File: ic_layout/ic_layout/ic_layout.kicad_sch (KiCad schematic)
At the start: 0 parts

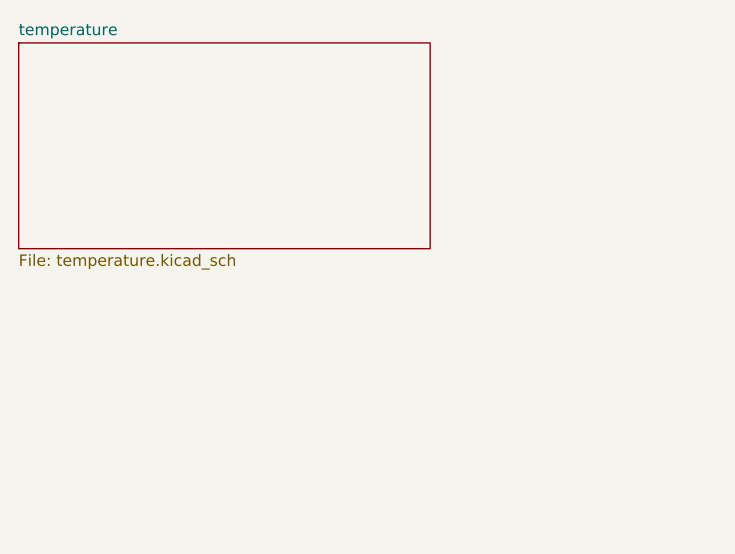
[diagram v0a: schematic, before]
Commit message: - Add XT30 - Add female ring terminal mount - Add 40A SMD fuse
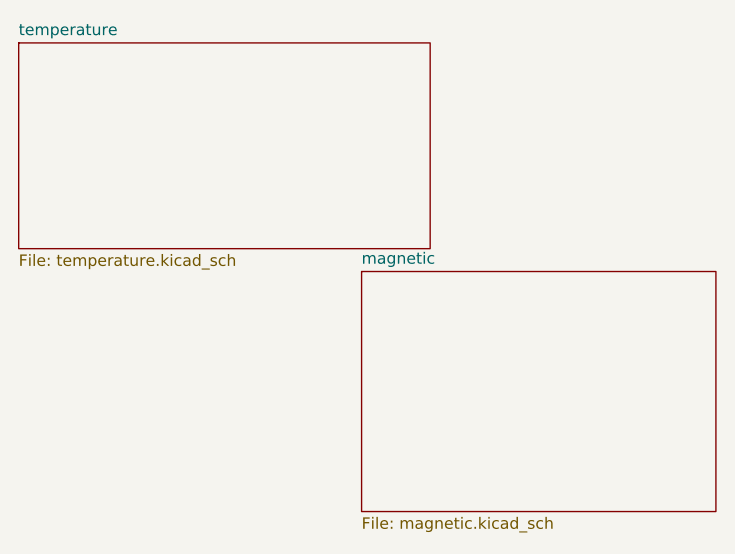
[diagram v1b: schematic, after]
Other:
- added sheet magnetic (magnetic.kicad_sch)
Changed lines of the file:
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@@
 	(paper "A4")
+	(sheet
+		(at 100.33 72.39)
+		(size 39.37 26.67)
+		(exclude_from_sim no)
+		(in_bom yes)
+		(on_board yes)
+		(dnp no)
+		(fields_autoplaced yes)
+		(stroke
+			(width 0.1524)
+			(type solid)
+		)
+		(fill
+			(color 0 0 0 0.0000)
+		)
+		(property "Sheetname" "magnetic"
+			(at 100.33 71.6784 0)
+			(effects
+				(font
+					(size 1.27 1.27)
+				)
+				(justify left bottom)
+			)
+		)
+		(property "Sheetfile" "magnetic.kicad_sch"
+			(at 100.33 99.6446 0)
+			(effects
+				(font
+					(size 1.27 1.27)
+				)
+				(justify left top)
+			)
+		)
+		(instances
+			(project "ic_layout"
+				(path "/8c701985-f320-40c9-85c5-5ea0cbfc0379"
+					(page "3")
+				)
+			)
+		)
+	)
 	(sheet
 		(at 62.23 46.99)
